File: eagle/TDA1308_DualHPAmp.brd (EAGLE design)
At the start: 35.9 x 66.8 mm, 28 parts, among them IC1 TDA1308, IC2 TDA1308

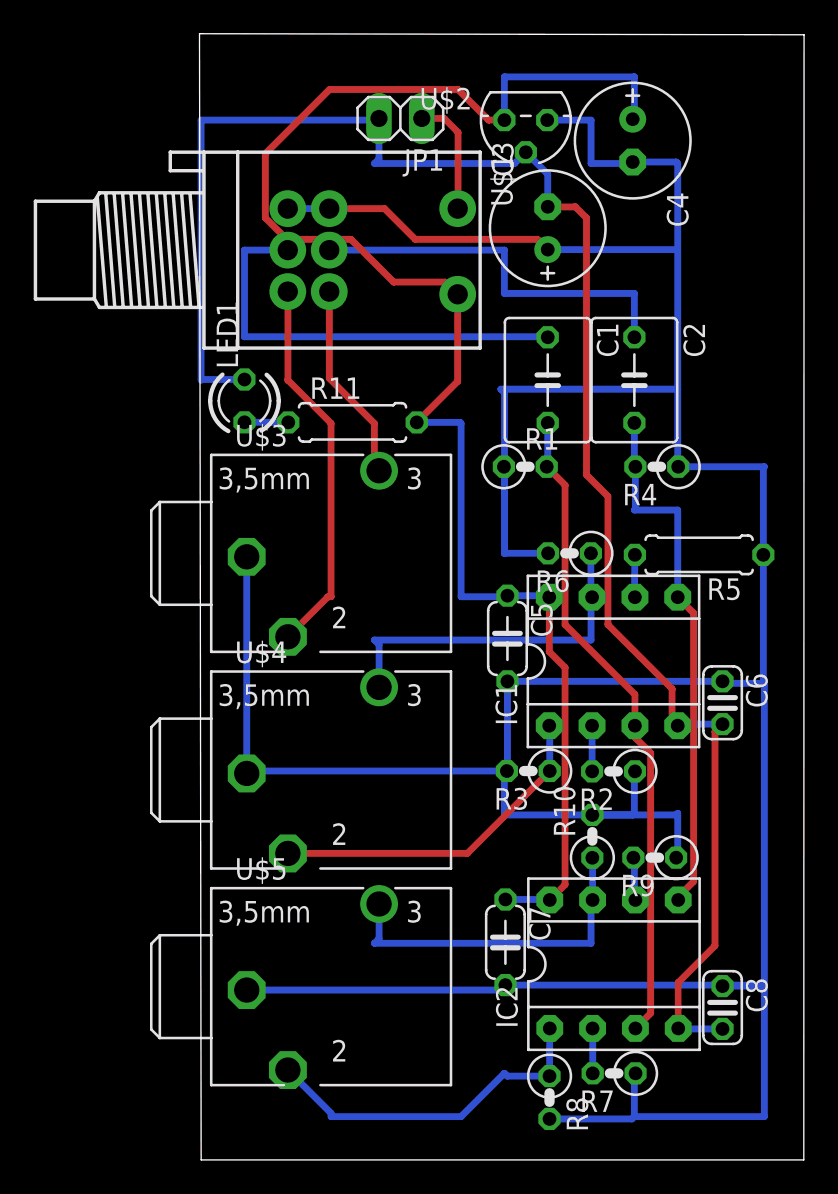
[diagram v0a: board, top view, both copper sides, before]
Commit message: 基板図修正（幅を削減）
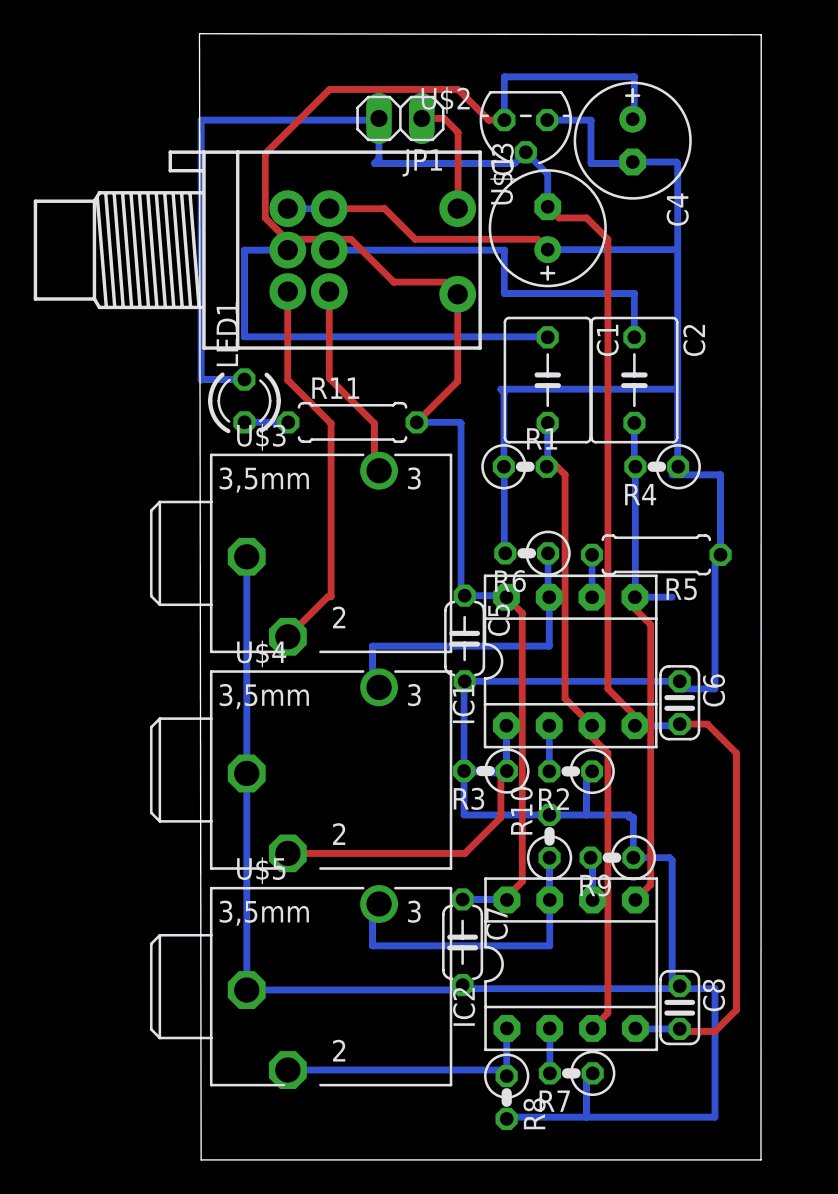
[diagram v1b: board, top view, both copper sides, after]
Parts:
- moved R5 2.54 mm to (27.0, 35.9)
- moved C5 2.54 mm to (15.6, 30.9)
- moved C7 2.54 mm to (15.5, 12.9)
- moved C6 2.54 mm to (28.4, 27.1)
- moved C8 2.54 mm to (28.4, 9.04)
- moved IC1 2.54 mm to (21.9, 29.6)
- moved IC2 2.54 mm to (21.9, 11.6)
- moved R10 2.54 mm to (20.7, 19.2)
- moved R2 2.54 mm to (21.9, 23.0)
- moved R3 2.54 mm to (16.9, 23.1)
- moved R6 2.54 mm to (19.3, 36.0)
- moved R7 2.54 mm to (22.0, 5.14)
- moved R8 2.54 mm to (18.1, 3.70)
- moved R9 2.54 mm to (24.4, 17.9)
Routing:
- net GND: track 242.8 -> 221.7 mm
- net N$16: track 20.7 -> 16.2 mm
- net VEE: track 103.9 -> 106.9 mm
- net VCC: track 94.7 -> 92.1 mm
- net N$11: track 21.0 -> 18.9 mm
- net N$8: track 20.3 -> 19.1 mm
- net N$18: track 20.7 -> 19.7 mm
- net N$6: track 38.9 -> 38.2 mm
- net N$7: track 2.72 -> 3.38 mm
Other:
- board size 35.9 x 66.8 mm -> 33.3 x 66.8 mm

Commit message: 基板図にグリッドを追加
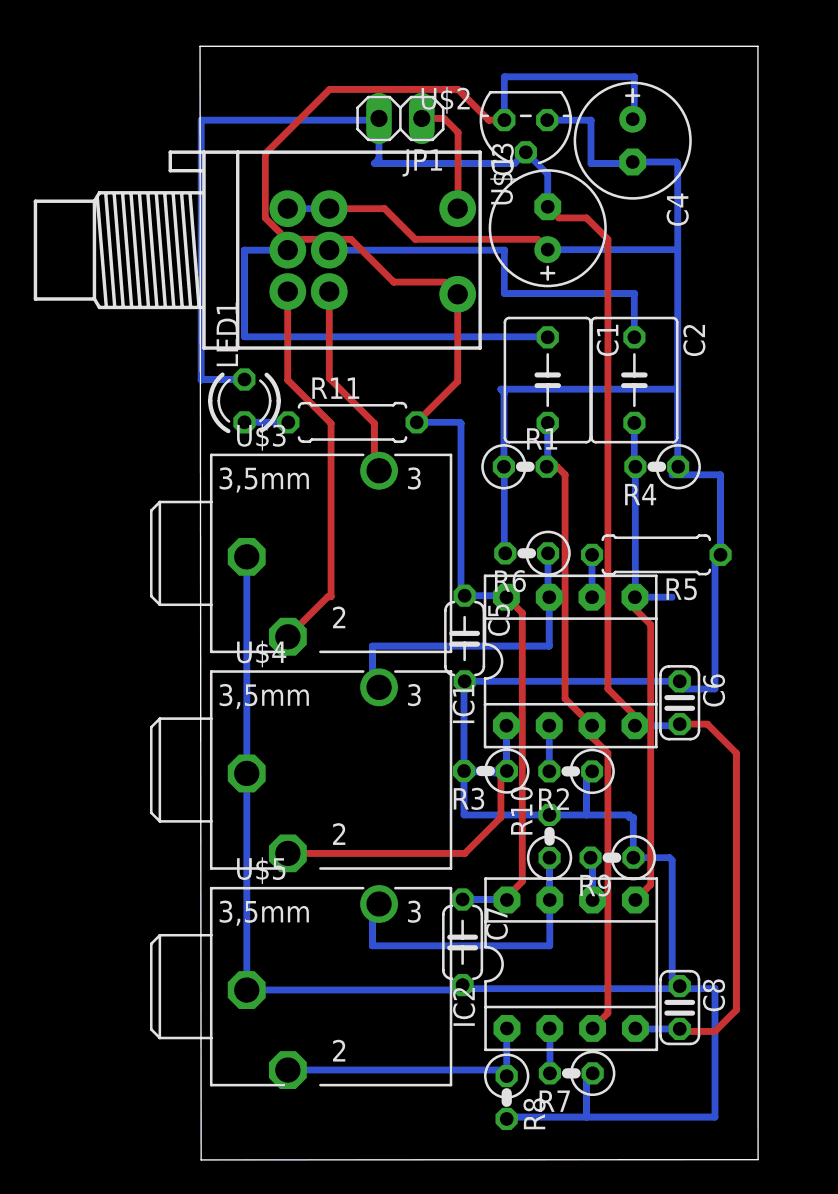
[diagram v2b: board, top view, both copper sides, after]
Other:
- board size 33.3 x 66.8 mm -> 33.1 x 66.1 mm
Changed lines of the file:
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@@
 <setting verticaltext="up"/>
 </settings>
-<grid distance="2.54" unitdist="mm" unit="mm" style="dots" multiple="1" display="yes" altdistance="1.27" altunitdist="mm" altunit="mm"/>
+<grid distance="2.54" unitdist="mm" unit="mm" style="lines" multiple="1" display="yes" altdistance="0.003125" altunitdist="mic" altunit="mm"/>
 <layers>
 <layer number="1" name="Top" color="4" fill="1" visible="yes" active="yes"/>
@@
 <layer number="97" name="Info" color="7" fill="1" visible="no" active="no"/>
 <layer number="98" name="Guide" color="6" fill="1" visible="no" active="no"/>
-<layer number="100" name="Grid" color="11" fill="1" visible="no" active="yes"/>
+<layer number="100" name="Grid" color="11" fill="1" visible="yes" active="yes"/>
 <layer number="101" name="Grid2" color="7" fill="1" visible="no" active="yes"/>
 <layer number="200" name="200bmp" color="1" fill="10" visible="no" active="no"/>
@@
 <board>
 <plain>
-<wire x1="0" y1="0" x2="33.21" y2="0" width="0" layer="20"/>
-<wire x1="33.21" y1="0" x2="33.224665625" y2="66.743490625" width="0" layer="20"/>
-<wire x1="33.224665625" y1="66.743490625" x2="-0.09671875" y2="66.806940625" width="0" layer="20"/>
-<wire x1="-0.09671875" y1="66.806940625" x2="0" y2="0" width="0" layer="20"/>
+<wire x1="0" y1="0" x2="33.037825" y2="0.01565" width="0" layer="20"/>
+<wire x1="33.037825" y1="0.01565" x2="33.029665625" y2="66.061684375" width="0" layer="20"/>
+<wire x1="33.029665625" y1="66.061684375" x2="-0.06421875" y2="66.060203125" width="0" layer="20"/>
+<wire x1="-0.06421875" y1="66.060203125" x2="0" y2="0" width="0" layer="20"/>
+<dimension x1="33.037825" y1="0.01565" x2="33.029665625" y2="66.061684375" x3="45.720625" y3="33.040234375" textsize="1.778" layer="1"/>
+<dimension x1="0" y1="0" x2="33.037825" y2="0.01565" x3="16.521321875" y3="-5.07939375" textsize="1.778" layer="1"/>
+<wire x1="35.56" y1="5.08" x2="0" y2="5.08" width="0" layer="100"/>
+<wire x1="35.56" y1="15.24" x2="0" y2="15.24" width="0" layer="100"/>
+<wire x1="35.56" y1="27.94" x2="0" y2="27.94" width="0" layer="100"/>
+<wire x1="35.56" y1="40.64" x2="0" y2="40.64" width="0" layer="100"/>
+<wire x1="35.56" y1="53.34" x2="0" y2="53.34" width="0" layer="100"/>
+<wire x1="35.56" y1="63.5" x2="0" y2="63.5" width="0" layer="100"/>
+<wire x1="12.7" y1="0" x2="12.7" y2="66.04" width="0" layer="100"/>
+<wire x1="22.86" y1="0" x2="25.4" y2="0" width="0" layer="100"/>
+<wire x1="25.4" y1="0" x2="25.4" y2="66.04" width="0" layer="100"/>
+<wire x1="35.56" y1="0" x2="35.56" y2="5.08" width="0" layer="100"/>
+<wire x1="35.56" y1="5.08" x2="35.56" y2="15.24" width="0" layer="100"/>
+<wire x1="35.56" y1="15.24" x2="35.56" y2="27.94" width="0" layer="100"/>
+<wire x1="35.56" y1="27.94" x2="35.56" y2="40.64" width="0" layer="100"/>
+<wire x1="35.56" y1="40.64" x2="35.56" y2="53.34" width="0" layer="100"/>
+<wire x1="35.56" y1="53.34" x2="35.56" y2="63.5" width="0" layer="100"/>
+<wire x1="35.56" y1="63.5" x2="35.56" y2="66.04" width="0" layer="100"/>
 </plain>
 <attributes>

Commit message: 基板図を修正
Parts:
- moved LED1 2.54 mm to (5.11, 45.0)
- moved R11 2.54 mm to (11.5, 43.8)
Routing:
- net VCC: track 92.1 -> 88.6 mm
- net VEE: track 106.9 -> 109.4 mm
- net N$1: track 22.7 -> 21.5 mm
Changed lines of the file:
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@@
 <setting verticaltext="up"/>
 </settings>
-<grid distance="2.54" unitdist="mm" unit="mm" style="lines" multiple="1" display="yes" altdistance="0.003125" altunitdist="mic" altunit="mm"/>
+<grid distance="2.54" unitdist="mm" unit="mm" style="lines" multiple="1" display="yes" altdistance="1.27" altunitdist="mm" altunit="mm"/>
 <layers>
 <layer number="1" name="Top" color="4" fill="1" visible="yes" active="yes"/>
@@
 <element name="R10" library="rcl" package="0207/2V" value="47k" x="20.6667125" y="19.19391875" rot="R90"/>
 <element name="JP1" library="pinhead" package="1X02" value="PWR" x="11.82" y="61.78" rot="R180"/>
-<element name="R11" library="rcl" package="0207/7" value="6.8k" x="8.98" y="43.75"/>
-<element name="LED1" library="led" package="LED3MM" value="Blue" x="2.570675" y="45.025459375" rot="R90"/>
+<element name="R11" library="rcl" package="0207/7" value="6.8k" x="11.52" y="43.75"/>
+<element name="LED1" library="led" package="LED3MM" value="Blue" x="5.110675" y="45.025459375" rot="R90"/>
 <element name="U$2" library="tle2426" package="TO226AA" value="TLE2426CLP" x="19.26" y="61.68" rot="R180"/>
 <element name="C3" library="rcl" package="E2,5-7" value="100u" x="20.56" y="55.27" rot="R90"/>
@@
 <contactref element="U$1" pad="1-3"/>
 <contactref element="U$3" pad="2"/>
-<wire x1="5.14" y1="51.51" x2="5.14" y2="46.26" width="0.4064" layer="1"/>
-<wire x1="5.14" y1="46.26" x2="7.71" y2="43.69" width="0.4064" layer="1"/>
-<wire x1="7.71" y1="43.69" x2="7.71" y2="33.41" width="0.4064" layer="1"/>
-<wire x1="7.71" y1="33.41" x2="7.525034375" y2="33.41" width="0.4064" layer="1"/>
-<wire x1="7.525034375" y1="33.41" x2="5.14689375" y2="31.031859375" width="0.4064" layer="1"/>
+<wire x1="5.14" y1="51.51" x2="5.14" y2="50.74" width="0.4064" layer="1"/>
+<wire x1="5.14" y1="50.74" x2="6.35" y2="49.53" width="0.4064" layer="1"/>
+<wire x1="6.35" y1="49.53" x2="6.35" y2="32.234965625" width="0.4064" layer="1"/>
+<wire x1="6.35" y1="32.234965625" x2="5.14689375" y2="31.031859375" width="0.4064" layer="1"/>
 </signal>
 <signal name="N$2">
 <contactref element="U$1" pad="2-3"/>
 <contactref element="U$3" pad="3"/>
-<wire x1="7.6" y1="51.51" x2="7.6" y2="46.37" width="0.4064" layer="1"/>
-<wire x1="7.6" y1="46.37" x2="10.28" y2="43.69" width="0.4064" layer="1"/>
-<wire x1="10.28" y1="43.69" x2="10.28" y2="41.157" width="0.4064" layer="1"/>
-<wire x1="10.28" y1="41.157" x2="10.5548" y2="40.8822" width="0.4064" layer="1"/>
+<wire x1="7.6" y1="51.51" x2="7.6" y2="50.82" width="0.4064" layer="1"/>
+<wire x1="7.6" y1="50.82" x2="10.16" y2="48.26" width="0.4064" layer="1"/>
+<wire x1="10.16" y1="48.26" x2="10.16" y2="41.277" width="0.4064" layer="1"/>
+<wire x1="10.16" y1="41.277" x2="10.5548" y2="40.8822" width="0.4064" layer="1"/>
 </signal>
 <signal name="GND">
@@
 <contactref element="JP1" pad="2"/>
 <contactref element="C8" pad="2"/>
-<wire x1="2.570675" y1="46.295459375" x2="0.035459375" y2="46.295459375" width="0.4064" layer="16"/>
+<wire x1="5.110675" y1="46.295459375" x2="0.035459375" y2="46.295459375" width="0.4064" layer="16"/>
 <wire x1="0.035459375" y1="46.295459375" x2="0" y2="46.26" width="0.4064" layer="16"/>
 <wire x1="0" y1="46.26" x2="0" y2="61.68" width="0.4064" layer="16"/>
@@
 <wire x1="25.7" y1="64.25" x2="25.7" y2="61.8357" width="0.4064" layer="16"/>
 <wire x1="25.7" y1="61.8357" x2="25.600615625" y2="61.736315625" width="0.4064" layer="16"/>
-<wire x1="12.79" y1="43.75" x2="15.36" y2="43.75" width="0.4064" layer="16"/>
-<wire x1="15.36" y1="43.75" x2="15.42" y2="43.69" width="0.4064" layer="16"/>
 <wire x1="15.42" y1="43.69" x2="15.42" y2="33.41" width="0.4064" layer="16"/>
 <wire x1="17.99" y1="61.68" x2="17.06" y2="61.68" width="0.4064" layer="1"/>
@@
 <wire x1="11.43" y1="52.07" x2="14.5" y2="52.07" width="0.4064" layer="1"/>
 <wire x1="14.5" y1="52.07" x2="15.22" y2="51.35" width="0.4064" layer="1"/>
-<wire x1="15.22" y1="51.35" x2="15.22" y2="46.18" width="0.4064" layer="1"/>
-<wire x1="15.22" y1="46.18" x2="12.79" y2="43.75" width="0.4064" layer="1"/>
 <wire x1="18.14" y1="15.42" x2="18.14" y2="15.6" width="0.4064" layer="1"/>
 <wire x1="18.14" y1="15.6" x2="19.05" y2="16.51" width="0.4064" layer="1"/>
@@
 <wire x1="15.63" y1="33.47" x2="15.48" y2="33.47" width="0.4064" layer="16"/>
 <wire x1="15.48" y1="33.47" x2="15.42" y2="33.41" width="0.4064" layer="16"/>
+<wire x1="15.22" y1="51.35" x2="15.22" y2="43.86" width="0.4064" layer="1"/>
+<wire x1="15.22" y1="43.86" x2="15.33" y2="43.75" width="0.4064" layer="1"/>
+<wire x1="15.42" y1="43.69" x2="15.39" y2="43.69" width="0.4064" layer="16"/>
+<wire x1="15.39" y1="43.69" x2="15.33" y2="43.75" width="0.4064" layer="16"/>
 </signal>
 <signal name="N$9">
@@
 <contactref element="R11" pad="1"/>
 <contactref element="LED1" pad="A"/>
-<wire x1="2.570675" y1="43.755459375" x2="5.164540625" y2="43.755459375" width="0.4064" layer="16"/>
-<wire x1="5.164540625" y1="43.755459375" x2="5.17" y2="43.75" width="0.4064" layer="16"/>
+<wire x1="5.110675" y1="43.755459375" x2="5.164540625" y2="43.755459375" width="0.4064" layer="16"/>
+<wire x1="5.164540625" y1="43.755459375" x2="7.71" y2="43.75" width="0.4064" layer="16"/>
 </signal>
 <signal name="N$10">

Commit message: Update
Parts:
- C2: value (none) -> 1uF
- R4: value 1uF -> 100k
- renumbered U$1 to POT1, U$2 to IC3, U$3 to JACK1, U$4 to JACK2, U$5 to JACK3
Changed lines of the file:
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@@
 <elements>
 <element name="C1" library="rcl" package="C050-050X075" value="1uF" x="20.56" y="46.26" rot="R270"/>
-<element name="C2" library="rcl" package="C050-050X075" value="" x="25.7" y="46.26" rot="R270"/>
+<element name="C2" library="rcl" package="C050-050X075" value="1uF" x="25.7" y="46.26" rot="R270"/>
 <element name="R1" library="rcl" package="0207/2V" value="100k" x="19.23" y="41.12"/>
-<element name="R4" library="rcl" package="0207/2V" value="1uF" x="27.03" y="41.12" rot="R180"/>
+<element name="R4" library="rcl" package="0207/2V" value="100k" x="27.03" y="41.12" rot="R180"/>
 <element name="IC1" library="burr-brown" package="DIL08" value="TDA1308" x="21.92" y="29.57">
 <attribute name="OC_NEWARK" value="74K3897" x="21.92" y="29.57" size="1.778" layer="27" display="off"/>
@@
 <element name="R11" library="rcl" package="0207/7" value="6.8k" x="11.52" y="43.75"/>
 <element name="LED1" library="led" package="LED3MM" value="Blue" x="5.110675" y="45.025459375" rot="R90"/>
-<element name="U$2" library="tle2426" package="TO226AA" value="TLE2426CLP" x="19.26" y="61.68" rot="R180"/>
+<element name="IC3" library="tle2426" package="TO226AA" value="TLE2426CLP" x="19.26" y="61.68" rot="R180"/>
 <element name="C3" library="rcl" package="E2,5-7" value="100u" x="20.56" y="55.27" rot="R90"/>
 <element name="C4" library="rcl" package="E2,5-7" value="100u" x="25.600615625" y="60.466315625" rot="R270"/>
@@
 <element name="C7" library="rcl" package="C050-024X044" value="0.1u" x="15.51" y="12.91" rot="R270"/>
 <element name="C8" library="rcl" package="C025-024X044" value="0.1u" x="28.39" y="9.04" rot="R270"/>
-<element name="U$1" library="mylib2" package="RK0971221" value="RK0971221" x="5.14" y="53.97" rot="R270"/>
-<element name="U$3" library="mylib2" package="MJ-3052W-0" value="MJ-353W-0" x="7.71" y="35.98"/>
-<element name="U$4" library="mylib2" package="MJ-3052W-0" value="MJ-353W-0" x="7.71" y="23.13"/>
-<element name="U$5" library="mylib2" package="MJ-3052W-0" value="MJ-353W-0" x="7.71" y="10.28"/>
+<element name="POT1" library="mylib2" package="RK0971221" value="RK0971221" x="5.14" y="53.97" rot="R270"/>
+<element name="JACK1" library="mylib2" package="MJ-3052W-0" value="MJ-353W-0" x="7.71" y="35.98"/>
+<element name="JACK2" library="mylib2" package="MJ-3052W-0" value="MJ-353W-0" x="7.71" y="23.13"/>
+<element name="JACK3" library="mylib2" package="MJ-3052W-0" value="MJ-353W-0" x="7.71" y="10.28"/>
 </elements>
 <signals>
 <signal name="N$1">
-<contactref element="U$1" pad="1-3"/>
-<contactref element="U$3" pad="2"/>
+<contactref element="POT1" pad="1-3"/>
+<contactref element="JACK1" pad="2"/>
 <wire x1="5.14" y1="51.51" x2="5.14" y2="50.74" width="0.4064" layer="1"/>
 <wire x1="5.14" y1="50.74" x2="6.35" y2="49.53" width="0.4064" layer="1"/>
@@
 </signal>
 <signal name="N$2">
-<contactref element="U$1" pad="2-3"/>
-<contactref element="U$3" pad="3"/>
+<contactref element="POT1" pad="2-3"/>
+<contactref element="JACK1" pad="3"/>
 <wire x1="7.6" y1="51.51" x2="7.6" y2="50.82" width="0.4064" layer="1"/>
 <wire x1="7.6" y1="50.82" x2="10.16" y2="48.26" width="0.4064" layer="1"/>
@@
 <contactref element="R9" pad="1"/>
 <contactref element="R10" pad="2"/>
-<contactref element="U$1" pad="1-1"/>
-<contactref element="U$1" pad="2-1"/>
-<contactref element="U$3" pad="1"/>
-<contactref element="U$4" pad="1"/>
-<contactref element="U$5" pad="1"/>
+<contactref element="POT1" pad="1-1"/>
+<contactref element="POT1" pad="2-1"/>
+<contactref element="JACK1" pad="1"/>
+<contactref element="JACK2" pad="1"/>
+<contactref element="JACK3" pad="1"/>
 <contactref element="C5" pad="2"/>
 <contactref element="C3" pad="+"/>
-<contactref element="U$2" pad="1"/>
+<contactref element="IC3" pad="1"/>
 <contactref element="C8" pad="1"/>
 <contactref element="C6" pad="1"/>
@@
 <signal name="N$3">
 <contactref element="C1" pad="1"/>
-<contactref element="U$1" pad="1-2"/>
+<contactref element="POT1" pad="1-2"/>
 <wire x1="5.14" y1="53.97" x2="2.57" y2="53.97" width="0.4064" layer="16"/>
 <wire x1="2.57" y1="53.97" x2="2.57" y2="48.83" width="0.4064" layer="16"/>
@@
 <signal name="N$4">
 <contactref element="C2" pad="1"/>
-<contactref element="U$1" pad="2-2"/>
+<contactref element="POT1" pad="2-2"/>
 <wire x1="7.6" y1="53.97" x2="17.99" y2="53.97" width="0.4064" layer="16"/>
 <wire x1="17.99" y1="53.97" x2="17.99" y2="51.4" width="0.4064" layer="16"/>
@@
 <contactref element="IC1" pad="1"/>
 <contactref element="R3" pad="1"/>
-<contactref element="U$4" pad="2"/>
+<contactref element="JACK2" pad="2"/>
 <wire x1="18.136984375" y1="23.0698625" x2="18.11" y2="23.0698625" width="0.4064" layer="16"/>
 <wire x1="18.11" y1="23.0698625" x2="18.11" y2="25.76" width="0.4064" layer="16"/>
@@
 <contactref element="LED1" pad="K"/>
 <contactref element="C6" pad="2"/>
-<contactref element="U$2" pad="2"/>
+<contactref element="IC3" pad="2"/>
 <contactref element="JP1" pad="2"/>
 <contactref element="C8" pad="2"/>
@@
 <contactref element="IC1" pad="8"/>
 <contactref element="IC2" pad="8"/>
-<contactref element="U$2" pad="3"/>
+<contactref element="IC3" pad="3"/>
 <contactref element="R11" pad="2"/>
 <contactref element="C5" pad="1"/>
 <contactref element="C7" pad="1"/>
 <contactref element="C4" pad="+"/>
-<contactref element="U$1" pad="3-2"/>
+<contactref element="POT1" pad="3-2"/>
 <wire x1="17.99" y1="61.68" x2="17.99" y2="64.25" width="0.4064" layer="16"/>
 <wire x1="17.99" y1="64.25" x2="25.7" y2="64.25" width="0.4064" layer="16"/>
@@
 <contactref element="IC1" pad="7"/>
 <contactref element="R6" pad="1"/>
-<contactref element="U$4" pad="3"/>
+<contactref element="JACK2" pad="3"/>
 <wire x1="20.65" y1="33.38" x2="20.581509375" y2="33.38" width="0.4064" layer="16"/>
 <wire x1="20.581509375" y1="33.38" x2="20.581509375" y2="35.98429375" width="0.4064" layer="16"/>
@@
 <contactref element="IC2" pad="1"/>
 <contactref element="R8" pad="1"/>
-<contactref element="U$5" pad="2"/>
+<contactref element="JACK3" pad="2"/>
 <wire x1="18.14" y1="7.8" x2="18.1258875" y2="7.8" width="0.4064" layer="16"/>
 <wire x1="18.1258875" y1="7.8" x2="18.1258875" y2="4.970959375" width="0.4064" layer="16"/>
@@
 <contactref element="IC2" pad="7"/>
 <contactref element="R10" pad="1"/>
-<contactref element="U$5" pad="3"/>
+<contactref element="JACK3" pad="3"/>
 <wire x1="20.68" y1="15.42" x2="20.32" y2="15.42" width="0.4064" layer="16"/>
 <wire x1="20.32" y1="15.42" x2="20.32" y2="15.24" width="0.4064" layer="16"/>
@@
 <signal name="N$10">
 <contactref element="JP1" pad="1"/>
-<contactref element="U$1" pad="3-1"/>
+<contactref element="POT1" pad="3-1"/>
 <wire x1="13.09" y1="61.78" x2="14.42" y2="61.78" width="0.4064" layer="1"/>
 <wire x1="14.42" y1="61.78" x2="15.24" y2="60.96" width="0.4064" layer="1"/>
